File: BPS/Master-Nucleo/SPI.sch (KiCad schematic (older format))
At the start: 37 parts, among them J7 VoltageSlaveConnector, J9 TempSlaveConnector, U11 Si8641EC-B-IS1, U12 SI8660EC-B-IS1, U15 RI3-1205S, U8 LTC6820, U9 HX1188FNL

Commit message: Connected all PCB components. Space in middle cannot be utilized. Distance between traces and copper must be less than .127mm or 5 mils according to manufacturer capabilities.
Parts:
- L4: symbol utsvt-bps:SRF0905-100Y -> BPS-Nucleo-rescue:SRF0905-100Y-utsvt-bps
- U12: symbol utsvt-bps:SI8660EC-B-IS1 -> BPS-Nucleo-rescue:SI8660EC-B-IS1-utsvt-bps
- U15: symbol utsvt-power-regulators:RI3-1205S -> BPS-Nucleo-rescue:RI3-1205S-utsvt-power-regulators
- U8: symbol utsvt-bps:LTC6820 -> BPS-Nucleo-rescue:LTC6820-utsvt-bps
- U9: symbol utsvt-bps:HX1188FNL -> BPS-Nucleo-rescue:HX1188FNL-utsvt-bps
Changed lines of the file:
@@
 EESchema Schematic File Version 4
 LIBS:BPS-Nucleo-cache
-EELAYER 26 0
+EELAYER 30 0
 EELAYER END
 $Descr A4 11693 8268
@@
 $EndDescr
 $Comp
-L utsvt-bps:LTC6820 U8
+L BPS-Nucleo-rescue:LTC6820-utsvt-bps U8
 U 1 1 5C4C8CC8
 P 3650 1700
@@
 If the wires lengths are short and you want to save more power, change IBIAS\nresistor to be 2.8k. Look in LTC6820 datasheet for more information on\ncalculating these BIAS resistors.
 $Comp
-L utsvt-bps:HX1188FNL U9
+L BPS-Nucleo-rescue:HX1188FNL-utsvt-bps U9
 U 1 1 5C4CE5A3
 P 8800 1700
@@
 	7500 3650 7600 3650
 $Comp
-L utsvt-bps:GND_A #PWR0160
+L BPS-Nucleo-rescue:GND_A-utsvt-bps #PWR0160
 U 1 1 5C3FE3B1
 P 8500 4550
@@
 	8500 4450 8500 4550
 $Comp
-L utsvt-bps:GND_A #PWR0161
+L BPS-Nucleo-rescue:GND_A-utsvt-bps #PWR0161
 U 1 1 5C407FF9
 P 9500 4450
@@
 	7500 3750 7500 3650
 $Comp
-L utsvt-bps:SI8660EC-B-IS1 U12
+L BPS-Nucleo-rescue:SI8660EC-B-IS1-utsvt-bps U12
 U 1 1 5C43A414
 P 8000 5200
@@
 	7400 6000 7500 6000
 $Comp
-L utsvt-bps:GND_A #PWR0167
+L BPS-Nucleo-rescue:GND_A-utsvt-bps #PWR0167
 U 1 1 5C528C84
 P 8600 6100
@@
 	9550 5900 9100 5900
 $Comp
-L utsvt-bps:GND_A #PWR0170
+L BPS-Nucleo-rescue:GND_A-utsvt-bps #PWR0170
 U 1 1 5C5CEB11
 P 9000 3650
@@
 NoConn ~ 7600 4150
 $Comp
-L utsvt-bps:GND_A #PWR0171
+L BPS-Nucleo-rescue:GND_A-utsvt-bps #PWR0171
 U 1 1 5CCE442E
 P 9200 5150
@@
 	1900 7450 2150 7450
 $Comp
-L utsvt-bps:SRF0905-100Y L?
+L BPS-Nucleo-rescue:SRF0905-100Y-utsvt-bps L?
 U 1 1 5C3DD0F6
 P 2400 7000
@@
 	3450 6600 3450 6700
 $Comp
-L utsvt-power-regulators:RI3-1205S U?
+L BPS-Nucleo-rescue:RI3-1205S-utsvt-power-regulators U?
 U 1 1 5C3DD149
 P 4000 7050
@@
 	4450 7350 4650 7350
 $Comp
-L utsvt-bps:GND_A #PWR0174
+L BPS-Nucleo-rescue:GND_A-utsvt-bps #PWR0174
 U 1 1 5C478A3F
 P 4650 7450
@@
 Wire Wire Line
 	7750 1400 8100 1400
-Wire Bus Line
-	6350 5400 6350 6000
-$Comp
-L power:+5V #PWR?
+$Comp
+L power:+5V #PWR0139
 U 1 1 5D8A9470
 P 2150 2250
-F 0 "#PWR?" H 2150 2100 50  0001 C CNN
+F 0 "#PWR0139" H 2150 2100 50  0001 C CNN
 F 1 "+5V" H 2165 2423 50  0000 C CNN
 F 2 "" H 2150 2250 50  0001 C CNN
@@
 	1    0    0    -1
 $EndComp
+Wire Bus Line
+	6350 5400 6350 6000
 $EndSCHEMATC

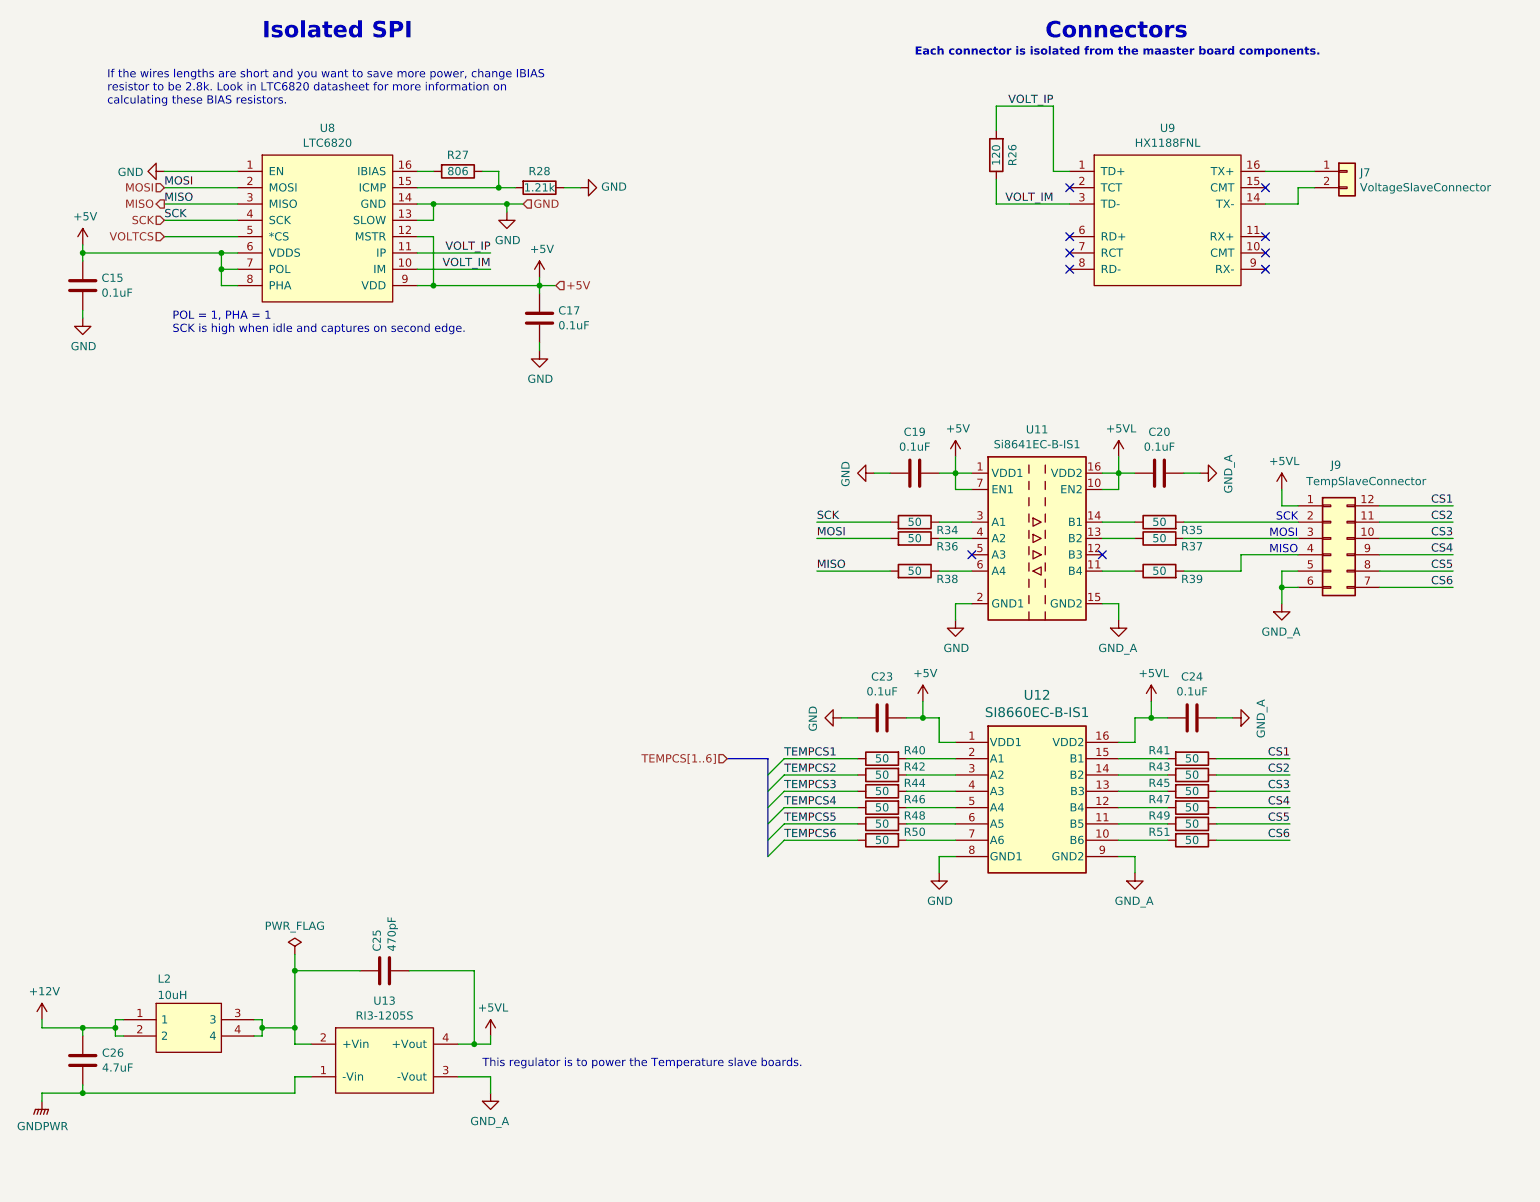
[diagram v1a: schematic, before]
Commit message: Before, components were outside board. Moved components to inside of board so usb port is unobstructed. Distance between copper and traces should be 5 mils.
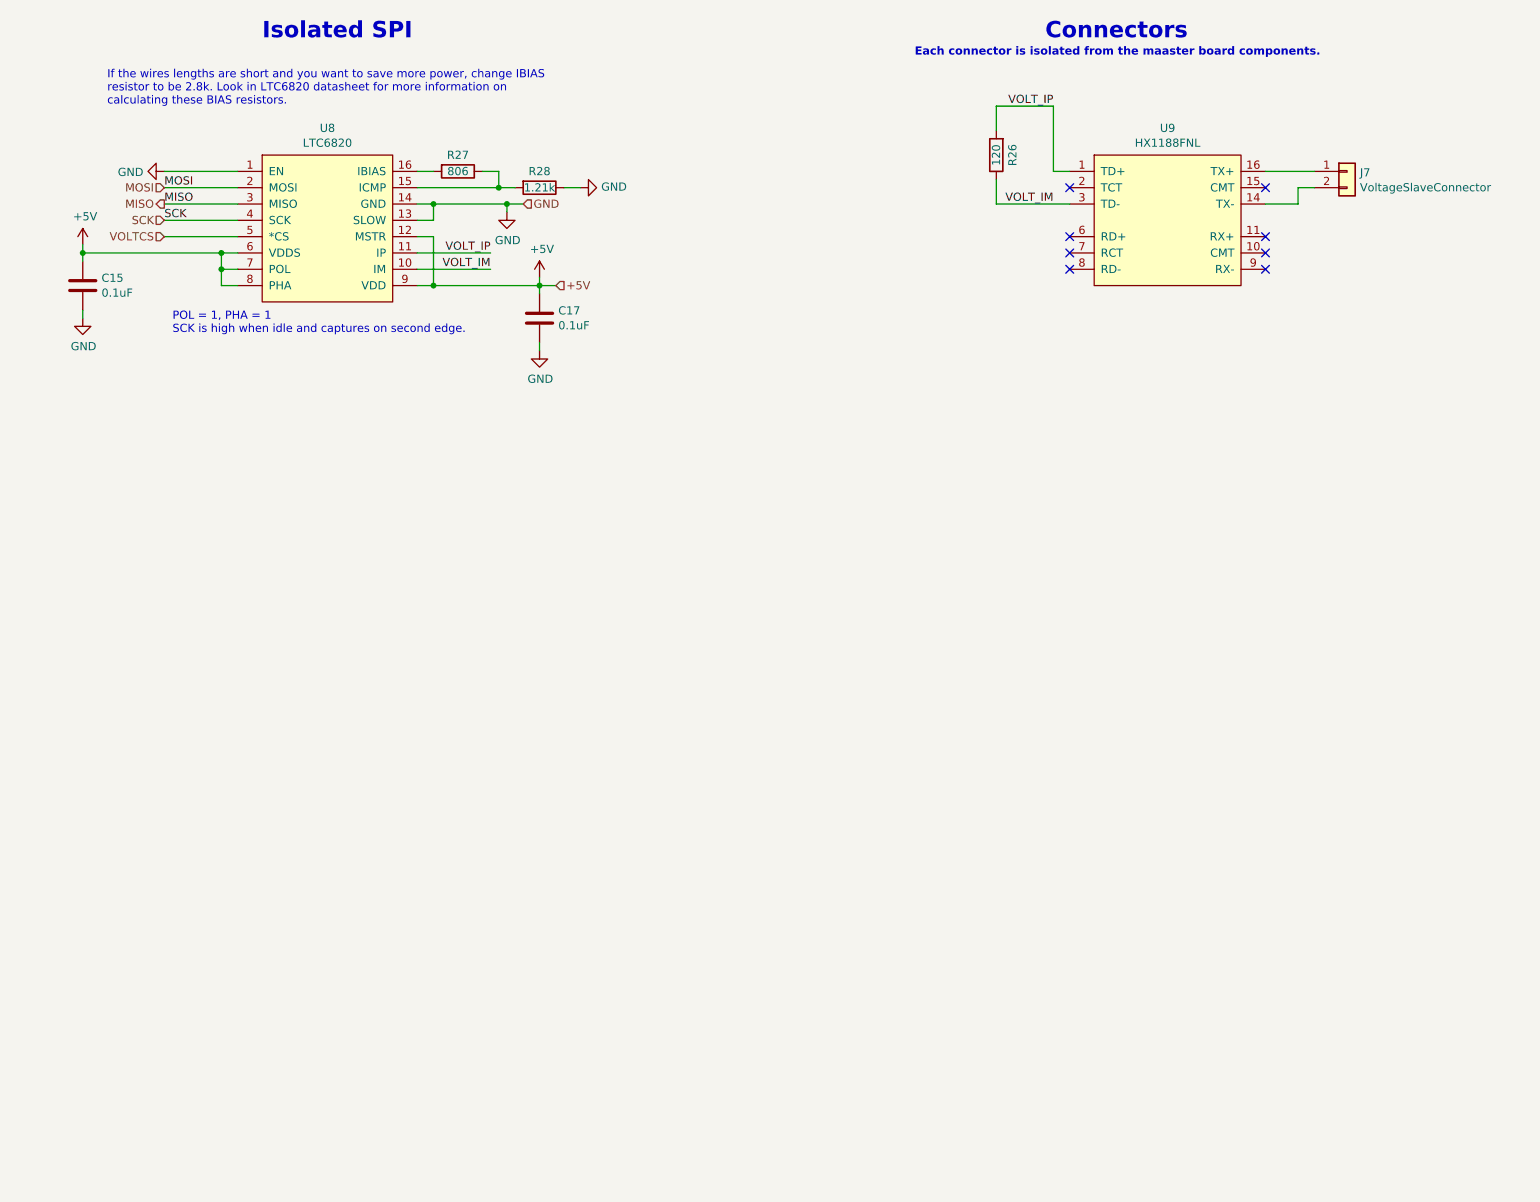
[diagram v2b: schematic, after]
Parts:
- removed C19, C20, C23, C24: 0.1uF, Capacitor_SMD:C_0805_2012Metric, symbol Device:C
- removed C46: 470pF, Capacitor_SMD:C_2220_5650Metric, symbol Device:C
- removed C47: 4.7uF, Capacitor_SMD:C_0805_2012Metric, symbol Device:C
- removed J9: TempSlaveConnector, UTSVT_Connectors:Molex_MicroFit3.0_2x6xP3.00mm_PolarizingPeg_Vertical, symbol Connector_Generic:Conn_02x06_Counter_Clockwise
- removed L4: 10uH, UTSVT_BPS:SRF0905A, symbol BPS-Nucleo-rescue:SRF0905-100Y-utsvt-bps
- removed R34, R35, R36, R37, R38, R39, R40, R41, R42, R43, R44, R45, R46, R47, R48, R49, R50, R51: 50, Resistor_SMD:R_0805_2012Metric, symbol Device:R
- removed U11: Si8641EC-B-IS1, Package_SO:SOIC-16_3.9x9.9mm_P1.27mm, symbol Isolator:Si8641EC-B-IS1
- removed U12: SI8660EC-B-IS1, Package_SO:SOIC-16_3.9x9.9mm_P1.27mm, symbol BPS-Nucleo-rescue:SI8660EC-B-IS1-utsvt-bps
- removed U15: RI3-1205S, UTSVT_ICs:RI3_DC_Converter, symbol BPS-Nucleo-rescue:RI3-1205S-utsvt-power-regulators
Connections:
- no-connect marks 10 -> 8
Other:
- note removed: "MISO"
- note removed: "MOSI"
- note removed: "SCK"
- note removed: "This regulator is to power the Temperature slave boards."
